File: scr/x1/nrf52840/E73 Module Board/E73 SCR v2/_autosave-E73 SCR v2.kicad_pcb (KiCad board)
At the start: 4 copper layers, 50 x 35 mm, 36 parts, among them J1 SWD, J2 USB_B_Micro, J3 XC1, J4 XC2, J5 XC3, J6 BAT, Q1 AO3401, SW1 SW_BAT, U1 E73-2G4M08S1C-52840, U2 MCP73831-2-OT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

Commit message: WIP v2
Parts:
- RST1: footprint Switches:Tac_SPST_RightAngle_SideActuated_THT -> Switches:Tac_SMD_6.4mm_Side_SPST_NO
- moved RST1 22.5 mm to (71.2, 122.5)
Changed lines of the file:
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@@
     (add_net "Net-(D1-Pad3)")
     (add_net "Net-(D2-Pad1)")
+    (add_net "Net-(D3-Pad1)")
     (add_net "Net-(D4-Pad1)")
+    (add_net "Net-(J1-Pad6)")
+    (add_net "Net-(J1-Pad7)")
+    (add_net "Net-(J1-Pad8)")
+    (add_net "Net-(J2-Pad4)")
     (add_net "Net-(J2-Pad6)")
     (add_net "Net-(R7-Pad2)")
@@
     (add_net P1.02)
     (add_net P1.09)
+    (add_net P1_11)
     (add_net RESET)
     (add_net SPKR)
@@
     (uvia_drill 0.1)
     (add_net VBUS)
+  )
+  (module Switches:Tac_SMD_6.4mm_Side_SPST_NO (layer F.Cu)
+    (at 71.25 122.5)
+    (descr "side smd tac switch")
+    (tags "switch tac rightangle side smd")
+    (attr smd)
+    (fp_text reference RST1 (at 0 0) (layer F.Fab)
+      (effects (font (size 1 1) (thickness 0.15)))
+    )
+    (fp_text value SW_SPST (at 0 -2.7) (layer F.Fab)
+      (effects (font (size 1 1) (thickness 0.15)))
+    )
+    (fp_line (start -1.3 2.5) (end 1.3 2.5) (layer Eco1.User) (width 0.15))
+    (fp_line (start 1.3 2.75) (end 1.3 1.75) (layer Eco1.User) (width 0.15))
+    (fp_line (start -1.3 2.75) (end 1.3 2.75) (layer Eco1.User) (width 0.15))
+    (fp_line (start -1.3 1.75) (end -1.3 2.75) (layer Eco1.User) (width 0.15))
+    (fp_line (start -3.4 1.75) (end -3.4 -1.7) (layer F.SilkS) (width 0.15))
+    (fp_line (start 3.4 1.75) (end -3.4 1.75) (layer F.SilkS) (width 0.15))
+    (fp_line (start 3.4 -1.75) (end 3.4 1.75) (layer F.SilkS) (width 0.15))
+    (fp_line (start -3.4 -1.75) (end 3.4 -1.75) (layer F.SilkS) (width 0.15))
+    (pad 1 smd rect (at 2.8 -0.85) (size 1.2 1) (layers F.Cu F.Paste F.Mask)
+      (net 1 GND))
+    (pad 2 smd rect (at 2.8 0.85) (size 1.2 1) (layers F.Cu F.Paste F.Mask)
+      (net 10 RESET))
+    (pad 2 smd rect (at -2.8 0.85) (size 1.2 1) (layers F.Cu F.Paste F.Mask)
+      (net 10 RESET))
+    (pad 1 smd rect (at -2.8 -0.75) (size 1.2 1) (layers F.Cu F.Paste F.Mask)
+      (net 1 GND))
+    (pad "" np_thru_hole circle (at 0 1.375) (size 0.75 0.75) (drill 0.75) (layers *.Cu *.Mask))
+    (pad "" np_thru_hole circle (at 0 -1.375) (size 0.75 0.75) (drill 0.75) (layers *.Cu *.Mask))
   )
   (module BVH_Components_Misc:SMD_Speaker (layer F.Cu)
@@
       (net 1 GND))
   )
-  (module Switches:Tac_SPST_RightAngle_SideActuated_THT (layer F.Cu)
-    (at 93.75 121.5)
-    (fp_text reference RST1 (at 0 2.9) (layer F.SilkS)
-      (effects (font (size 1 1) (thickness 0.15)))
-    )
-    (fp_text value SW_SPST (at -0.1 -0.2) (layer F.Fab)
-      (effects (font (size 1 1) (thickness 0.15)))
-    )
-    (fp_line (start -1.75 6.25) (end -1.75 2) (layer F.CrtYd) (width 0.15))
-    (fp_line (start 1.75 6.25) (end 1.75 2) (layer F.CrtYd) (width 0.15))
-    (fp_text user "Button Front" (at 0.05 5.65) (layer Dwgs.User)
-      (effects (font (size 1 1) (thickness 0.15)))
-    )
-    (fp_line (start -1.75 6.25) (end 1.75 6.25) (layer F.CrtYd) (width 0.15))
-    (fp_line (start -5 2) (end -5 -3.45) (layer F.CrtYd) (width 0.15))
-    (fp_line (start 5 2) (end -5 2) (layer F.CrtYd) (width 0.15))
-    (fp_line (start 4.95 -3.5) (end 4.95 2) (layer F.CrtYd) (width 0.15))
-    (fp_line (start -5 -3.5) (end 4.95 -3.5) (layer F.CrtYd) (width 0.15))
-    (pad "" thru_hole oval (at 3.5 -1.25) (size 2 2.5) (drill 1.3) (layers *.Cu *.Mask))
-    (pad 2 thru_hole oval (at 2.25 1.25) (size 1.5 1.5) (drill 1) (layers *.Cu *.Mask)
-      (net 10 RESET))
-    (pad "" thru_hole oval (at -3.5 -1.25) (size 2 2.5) (drill 1.3) (layers *.Cu *.Mask))
-    (pad 1 thru_hole oval (at -2.25 1.24) (size 1.5 1.5) (drill 1) (layers *.Cu *.Mask)
-      (net 1 GND))
-  )

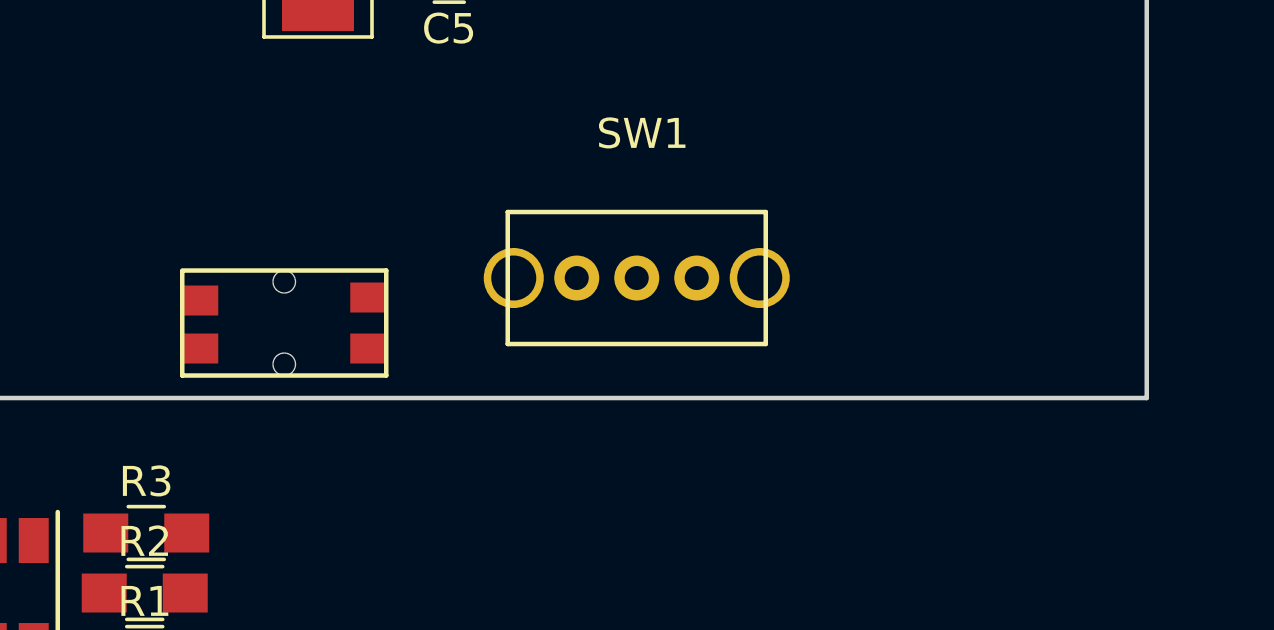
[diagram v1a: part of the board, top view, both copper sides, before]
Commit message: Initial project structure for nrf sdk application
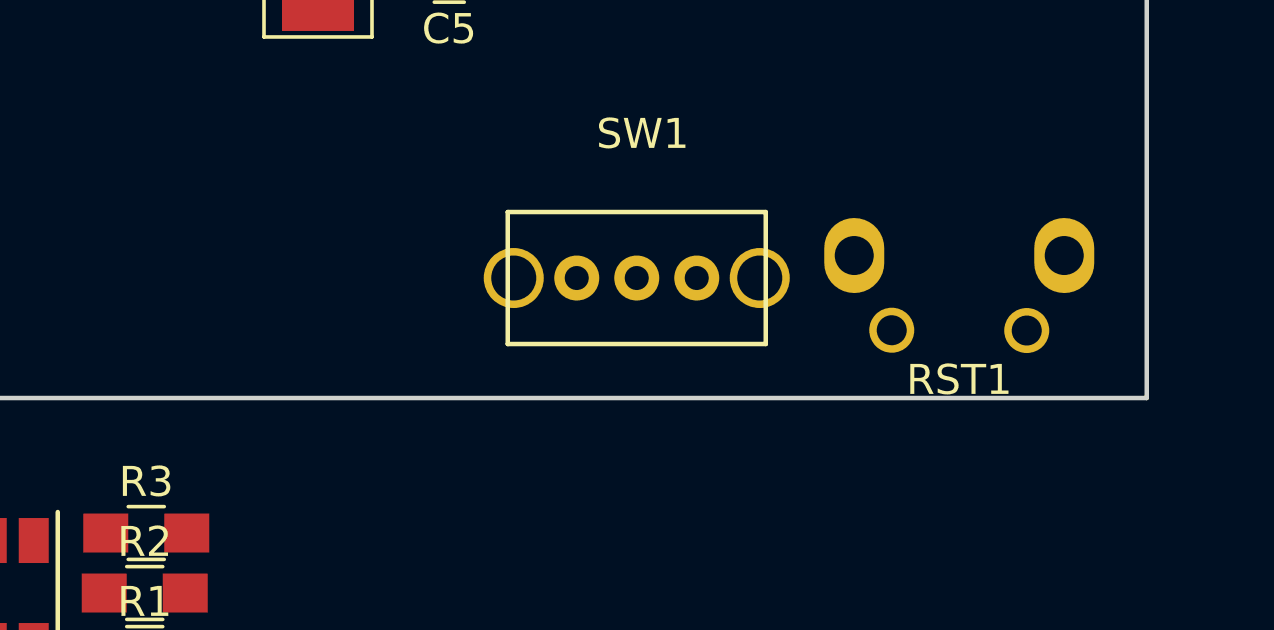
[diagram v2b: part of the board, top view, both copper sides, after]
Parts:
- RST1: footprint Switches:Tac_SMD_6.4mm_Side_SPST_NO -> Switches:Tac_SPST_RightAngle_SideActuated_THT
- moved RST1 22.5 mm to (93.8, 121.5)
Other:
- net class Default: clearance 0.2 -> 0.2032; trace_width 0.25 -> 0.508
- net class GND added: clearance 0.2, trace_width 0.381, via_dia 0.8, via_drill 0.4
- net class VBUS: clearance 0.25 -> 0.254; trace_width 0.3 -> 0.381
- net class VCC added: clearance 0.254, trace_width 0.381, via_dia 0.8, via_drill 0.4
- rule trace_clearance: 0.2 -> 0.2032
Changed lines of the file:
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@@
-(kicad_pcb (version 20171130) (host pcbnew 5.1.5-52549c5~86~ubuntu18.04.1)
+(kicad_pcb (version 20171130) (host pcbnew "(5.1.5-0-10_14)")
   (general
     (thickness 1.6)
@@
   )
   (setup
-    (last_trace_width 0.25)
-    (trace_clearance 0.2)
+    (last_trace_width 0.508)
+    (trace_clearance 0.2032)
     (zone_clearance 0.508)
     (zone_45_only no)
@@
   (net 40 "Net-(R9-Pad2)")
   (net_class Default "This is the default net class."
-    (clearance 0.2)
-    (trace_width 0.25)
+    (clearance 0.2032)
+    (trace_width 0.508)
     (via_dia 0.8)
     (via_drill 0.4)
     (uvia_dia 0.3)
     (uvia_drill 0.1)
-    (add_net +3V3)
-    (add_net +BATT)
     (add_net BATSENSE)
     (add_net D+)
     (add_net D-)
-    (add_net GND)
     (add_net LED_1)
     (add_net LED_B)
@@
     (add_net "Net-(D1-Pad3)")
     (add_net "Net-(D2-Pad1)")
-    (add_net "Net-(D3-Pad1)")
     (add_net "Net-(D4-Pad1)")
-    (add_net "Net-(J1-Pad6)")
-    (add_net "Net-(J1-Pad7)")
-    (add_net "Net-(J1-Pad8)")
-    (add_net "Net-(J2-Pad4)")
     (add_net "Net-(J2-Pad6)")
     (add_net "Net-(R7-Pad2)")
@@
     (add_net "Net-(RPROG1-Pad1)")
     (add_net "Net-(SW1-Pad2)")
-    (add_net "Net-(U1-Pad12)")
-    (add_net "Net-(U1-Pad14)")
-    (add_net "Net-(U1-Pad2)")
-    (add_net "Net-(U1-Pad25)")
-    (add_net "Net-(U1-Pad3)")
-    (add_net "Net-(U1-Pad32)")
-    (add_net "Net-(U1-Pad33)")
-    (add_net "Net-(U1-Pad40)")
-    (add_net "Net-(U1-Pad41)")
-    (add_net "Net-(U1-Pad43)")
-    (add_net "Net-(U1-Pad6)")
-    (add_net "Net-(U3-Pad4)")
     (add_net P.04_A2)
     (add_net P0.05_A3)
@@
     (add_net P1.02)
     (add_net P1.09)
-    (add_net P1_11)
     (add_net RESET)
     (add_net SPKR)
@@
     (add_net XL2)
   )
+  (net_class GND ""
+    (clearance 0.2)
+    (trace_width 0.381)
+    (via_dia 0.8)
+    (via_drill 0.4)
+    (uvia_dia 0.3)
+    (uvia_drill 0.1)
+    (add_net GND)
+  )
   (net_class VBUS ""
-    (clearance 0.25)
-    (trace_width 0.3)
+    (clearance 0.254)
+    (trace_width 0.381)
     (via_dia 0.8)
     (via_drill 0.4)
@@
     (add_net VBUS)
   )
-  (module Switches:Tac_SMD_6.4mm_Side_SPST_NO (layer F.Cu)
-    (at 71.25 122.5)
-    (descr "side smd tac switch")
-    (tags "switch tac rightangle side smd")
-    (attr smd)
-    (fp_text reference RST1 (at 0 0) (layer F.Fab)
-      (effects (font (size 1 1) (thickness 0.15)))
-    )
-    (fp_text value SW_SPST (at 0 -2.7) (layer F.Fab)
-      (effects (font (size 1 1) (thickness 0.15)))
-    )
-    (fp_line (start -1.3 2.5) (end 1.3 2.5) (layer Eco1.User) (width 0.15))
-    (fp_line (start 1.3 2.75) (end 1.3 1.75) (layer Eco1.User) (width 0.15))
-    (fp_line (start -1.3 2.75) (end 1.3 2.75) (layer Eco1.User) (width 0.15))
-    (fp_line (start -1.3 1.75) (end -1.3 2.75) (layer Eco1.User) (width 0.15))
-    (fp_line (start -3.4 1.75) (end -3.4 -1.7) (layer F.SilkS) (width 0.15))
-    (fp_line (start 3.4 1.75) (end -3.4 1.75) (layer F.SilkS) (width 0.15))
-    (fp_line (start 3.4 -1.75) (end 3.4 1.75) (layer F.SilkS) (width 0.15))
-    (fp_line (start -3.4 -1.75) (end 3.4 -1.75) (layer F.SilkS) (width 0.15))
-    (pad 1 smd rect (at 2.8 -0.85) (size 1.2 1) (layers F.Cu F.Paste F.Mask)
-      (net 1 GND))
-    (pad 2 smd rect (at 2.8 0.85) (size 1.2 1) (layers F.Cu F.Paste F.Mask)
-      (net 10 RESET))
-    (pad 2 smd rect (at -2.8 0.85) (size 1.2 1) (layers F.Cu F.Paste F.Mask)
-      (net 10 RESET))
-    (pad 1 smd rect (at -2.8 -0.75) (size 1.2 1) (layers F.Cu F.Paste F.Mask)
-      (net 1 GND))
-    (pad "" np_thru_hole circle (at 0 1.375) (size 0.75 0.75) (drill 0.75) (layers *.Cu *.Mask))
-    (pad "" np_thru_hole circle (at 0 -1.375) (size 0.75 0.75) (drill 0.75) (layers *.Cu *.Mask))
+  (net_class VCC ""
+    (clearance 0.254)
+    (trace_width 0.381)
+    (via_dia 0.8)
+    (via_drill 0.4)
+    (uvia_dia 0.3)
+    (uvia_drill 0.1)
+    (add_net +3V3)
+    (add_net +BATT)
   )
   (module BVH_Components_Misc:SMD_Speaker (layer F.Cu)
@@
       (net 1 GND))
   )
+  (module Switches:Tac_SPST_RightAngle_SideActuated_THT (layer F.Cu)
+    (at 93.75 121.5)
+    (fp_text reference RST1 (at 0 2.9) (layer F.SilkS)
+      (effects (font (size 1 1) (thickness 0.15)))
+    )
+    (fp_text value SW_SPST (at -0.1 -0.2) (layer F.Fab)
+      (effects (font (size 1 1) (thickness 0.15)))
+    )
+    (fp_line (start -1.75 6.25) (end -1.75 2) (layer F.CrtYd) (width 0.15))
+    (fp_line (start 1.75 6.25) (end 1.75 2) (layer F.CrtYd) (width 0.15))
+    (fp_text user "Button Front" (at 0.05 5.65) (layer Dwgs.User)
+      (effects (font (size 1 1) (thickness 0.15)))
+    )
+    (fp_line (start -1.75 6.25) (end 1.75 6.25) (layer F.CrtYd) (width 0.15))
+    (fp_line (start -5 2) (end -5 -3.45) (layer F.CrtYd) (width 0.15))
+    (fp_line (start 5 2) (end -5 2) (layer F.CrtYd) (width 0.15))
+    (fp_line (start 4.95 -3.5) (end 4.95 2) (layer F.CrtYd) (width 0.15))
+    (fp_line (start -5 -3.5) (end 4.95 -3.5) (layer F.CrtYd) (width 0.15))
+    (pad "" thru_hole oval (at 3.5 -1.25) (size 2 2.5) (drill 1.3) (layers *.Cu *.Mask))
+    (pad 2 thru_hole oval (at 2.25 1.25) (size 1.5 1.5) (drill 1) (layers *.Cu *.Mask)
+      (net 10 RESET))
+    (pad "" thru_hole oval (at -3.5 -1.25) (size 2 2.5) (drill 1.3) (layers *.Cu *.Mask))
+    (pad 1 thru_hole oval (at -2.25 1.24) (size 1.5 1.5) (drill 1) (layers *.Cu *.Mask)
+      (net 1 GND))
+  )
